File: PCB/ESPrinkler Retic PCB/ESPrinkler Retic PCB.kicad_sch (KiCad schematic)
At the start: 0 parts

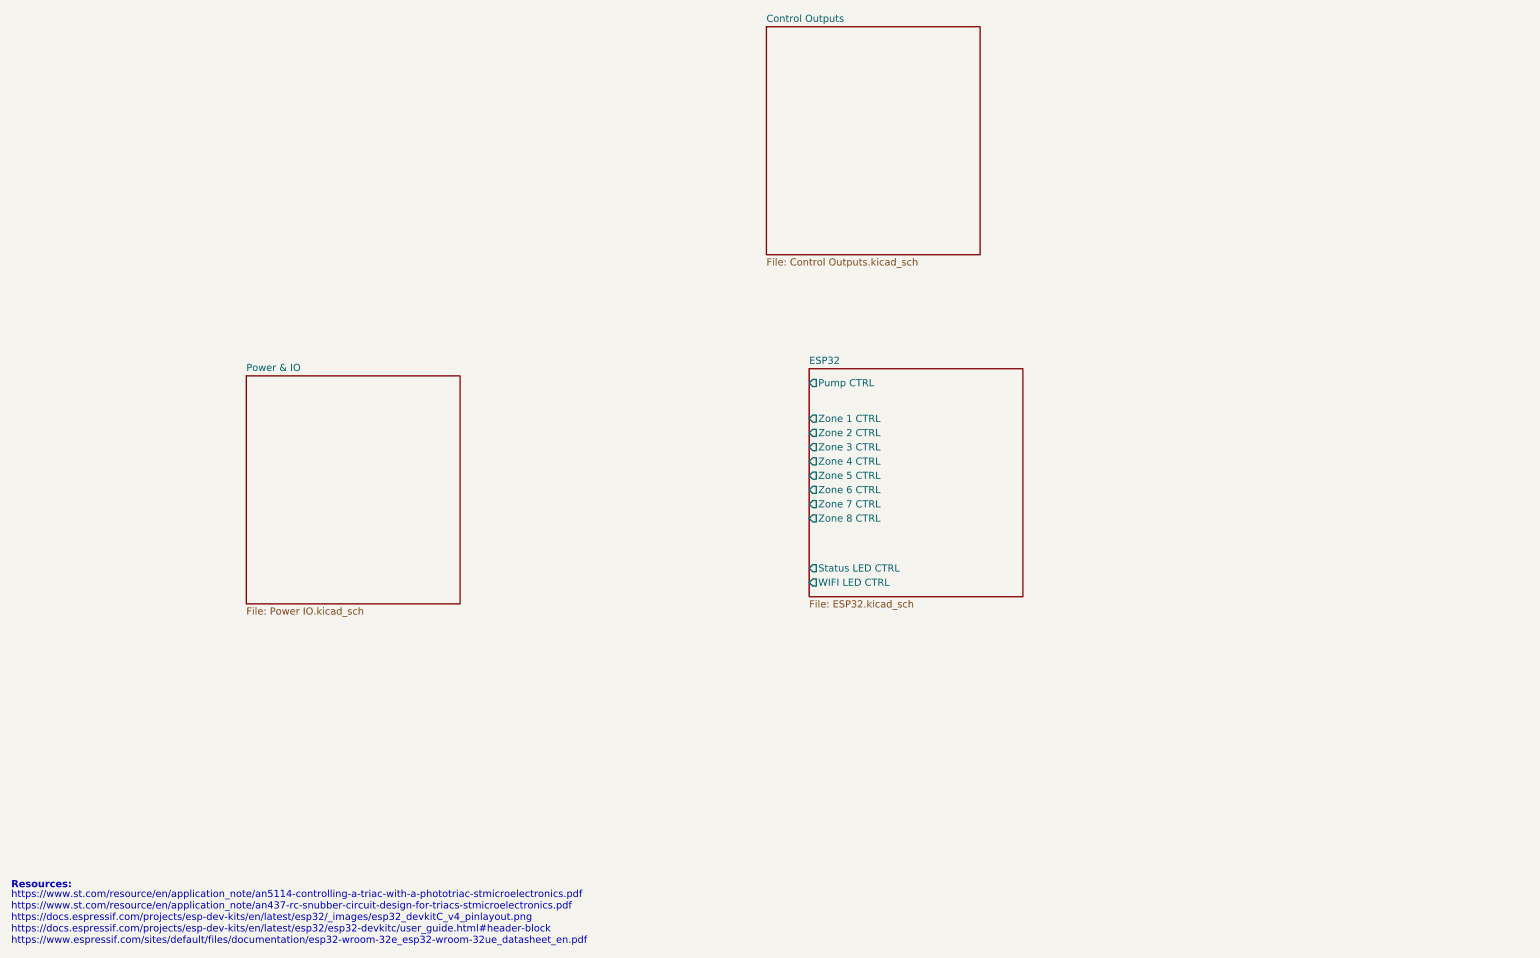
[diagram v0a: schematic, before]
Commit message: Initial schematic design completed
Finish initial schematic design and source all required components. DRC completed with only minor warnings (regarding net names, no worries). Move on to begin PCB design
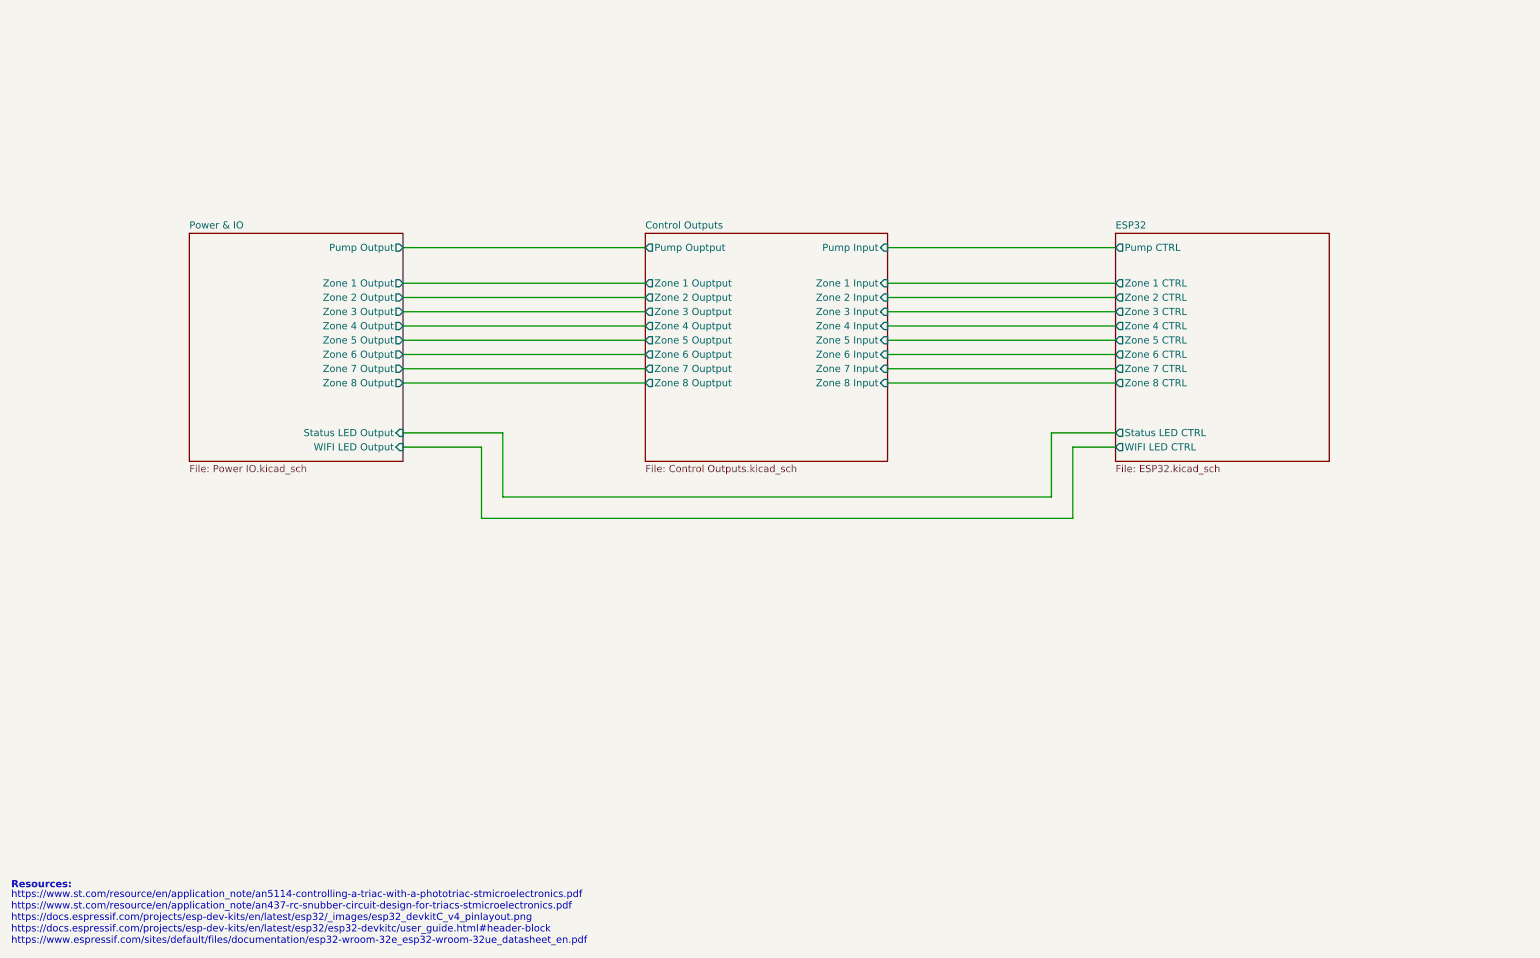
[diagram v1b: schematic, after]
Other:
- sheet Control Outputs ports: added Pump Input, Pump Ouptput, Zone 1 Input, Zone 1 Ouptput, Zone 2 Input, Zone 2 Ouptput, Zone 3 Input, Zone 3 Ouptput, Zone 4 Input, Zone 4 Ouptput, Zone 5 Input, Zone 5 Ouptput, Zone 6 Input, Zone 6 Ouptput, Zone 7 Input, Zone 7 Ouptput, Zone 8 Input, Zone 8 Ouptput; removed none
- sheet Power & IO ports: added Pump Output, Status LED Output, WIFI LED Output, Zone 1 Output, Zone 2 Output, Zone 3 Output, Zone 4 Output, Zone 5 Output, Zone 6 Output, Zone 7 Output, Zone 8 Output; removed none

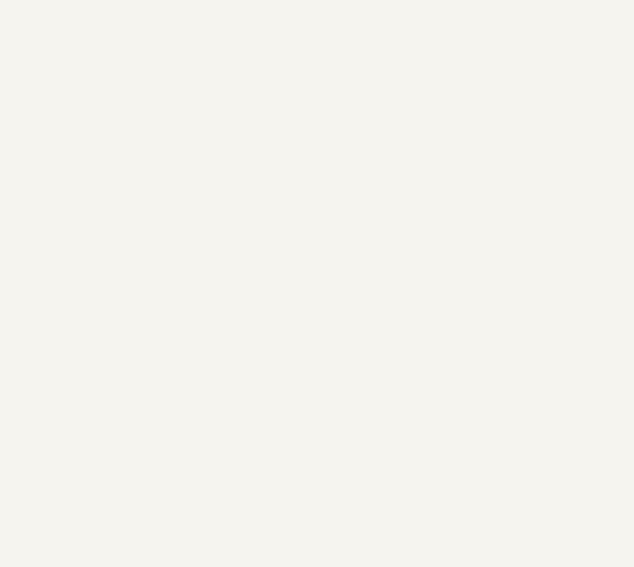
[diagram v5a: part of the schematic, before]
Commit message: Change mounting holes
Change mounting holes to M3.2 with exposed pads and vias. Add them to schematic for reference
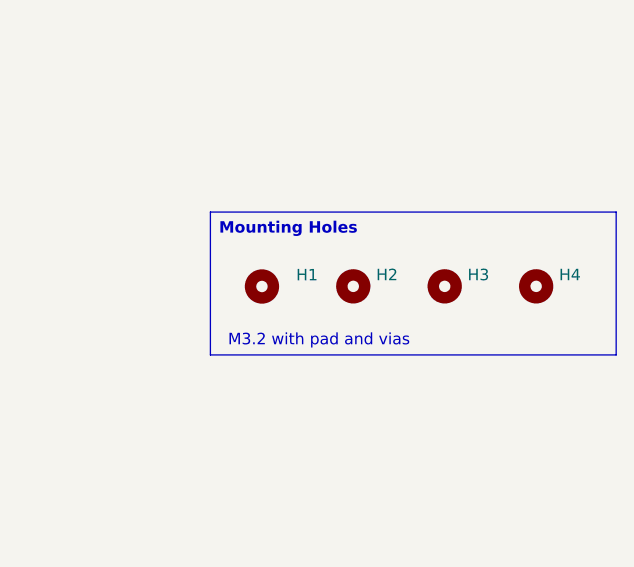
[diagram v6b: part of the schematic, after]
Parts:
- added H1, H2, H3, H4: MountingHole, MountingHole:MountingHole_3.2mm_M3_Pad_Via, symbol Mechanical:MountingHole
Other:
- note added: "M3.2 with pad and vias"
